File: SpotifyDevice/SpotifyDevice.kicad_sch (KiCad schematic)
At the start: 0 parts

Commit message: Found Draft 1 Parts and imported Libraries
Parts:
- added S1: B3F-4055, ImportedParts:SW_B3F-4055, symbol Imported Parts:B3F-4055
- added U1: ESP32-S3-WROOM-1, RF_Module:ESP32-S3-WROOM-1, symbol RF_Module:ESP32-S3-WROOM-1
- added U2: CR2013-MI2120, Display:CR2013-MI2120, symbol Driver_Display:CR2013-MI2120
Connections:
- new net: S1.1, S1.2
- new net: S1.3, S1.4
- new net: U1.1 (GND), U1.40 (GND), U1.41 (GND)

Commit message: Draft 1 of Schematic Complete
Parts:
- added C1, C2, C4: 0.1 μF, symbol Device:C_Small_US
- added C3: 10 μF, symbol Device:C_Small_US
- added D1: LED, symbol Device:LED
- added R1: 10kΩ, symbol Device:R_Small_US
- added R2: 330Ω, symbol Device:R_Small_US
- added S2, S3, S4, S5: B3F-4055, ImportedParts:SW_B3F-4055, symbol Imported Parts:B3F-4055
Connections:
- net S1: now reaches S1.1, S1.2
- net S1: now also U1.7 (IO7)
- net GND: now reaches S1.3, S1.4
- net GND: now also U1.1 (GND), U1.40 (GND), U1.41 (GND), U2.2 (GND), C1.1, C2.1, C3.1, C4.1, D1.1 (K), S2.3, S2.4, S3.3, S3.4, S4.3, S4.4, S5.3, S5.4
- net S2: now reaches U1.12 (IO8)
- net S2: now also S2.1, S2.2
- net S3: now reaches U1.17 (IO9)
- net S3: now also S3.1, S3.2
- net S4: now reaches U1.18 (IO10)
- net S4: now also S4.1, S4.2
- net S5: now reaches U1.19 (IO11)
- net S5: now also S5.1, S5.2
- net +3.3V: now reaches U1.2 (3V3)
- net +3.3V: now also U2.1 (VCC), U2.8 (LED), C1.2, C2.2, C3.2, R1.2
- net at U1.20 (IO12): now also R2.2
- net MOSI: now reaches U1.28 (IO35)
- net MOSI: now also U2.6 (MOSI)
- net SCK: now reaches U1.29 (IO36)
- net SCK: now also U2.7 (SCK)
- net at U1.3 (EN): now also C4.2, R1.1
- net D/C: now reaches U1.30 (IO37)
- net D/C: now also U2.5 (D/~{C})
- net CS: now reaches U1.31 (IO38)
- net CS: now also U2.3 (~{CS})
- net RESET: now reaches U1.32 (IO39)
- net RESET: now also U2.4 (RESET)
- new net LED: D1.2 (A), R2.1
- no-connect marks 0 -> 31
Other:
- note added: "AddOns"
- note added: "Microcontroller"
- note added: "Screen"
- moved on the sheet: S1, U1, U2

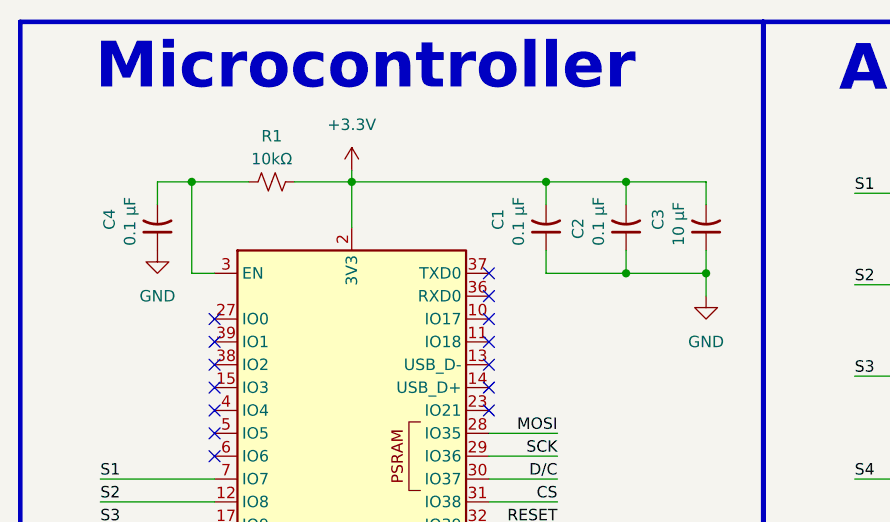
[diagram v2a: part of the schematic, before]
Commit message: Added 3D models and updated SCM
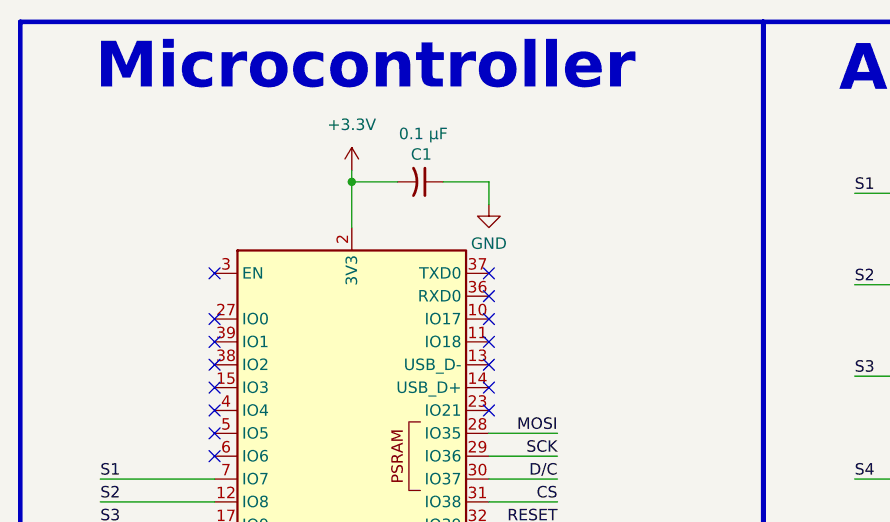
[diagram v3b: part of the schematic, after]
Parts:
- removed C2, C4: 0.1 μF, symbol Device:C_Small_US
- removed C3: 10 μF, symbol Device:C_Small_US
- removed R1: 10kΩ, symbol Device:R_Small_US
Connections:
- no-connect marks 31 -> 32
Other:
- moved on the sheet: C1

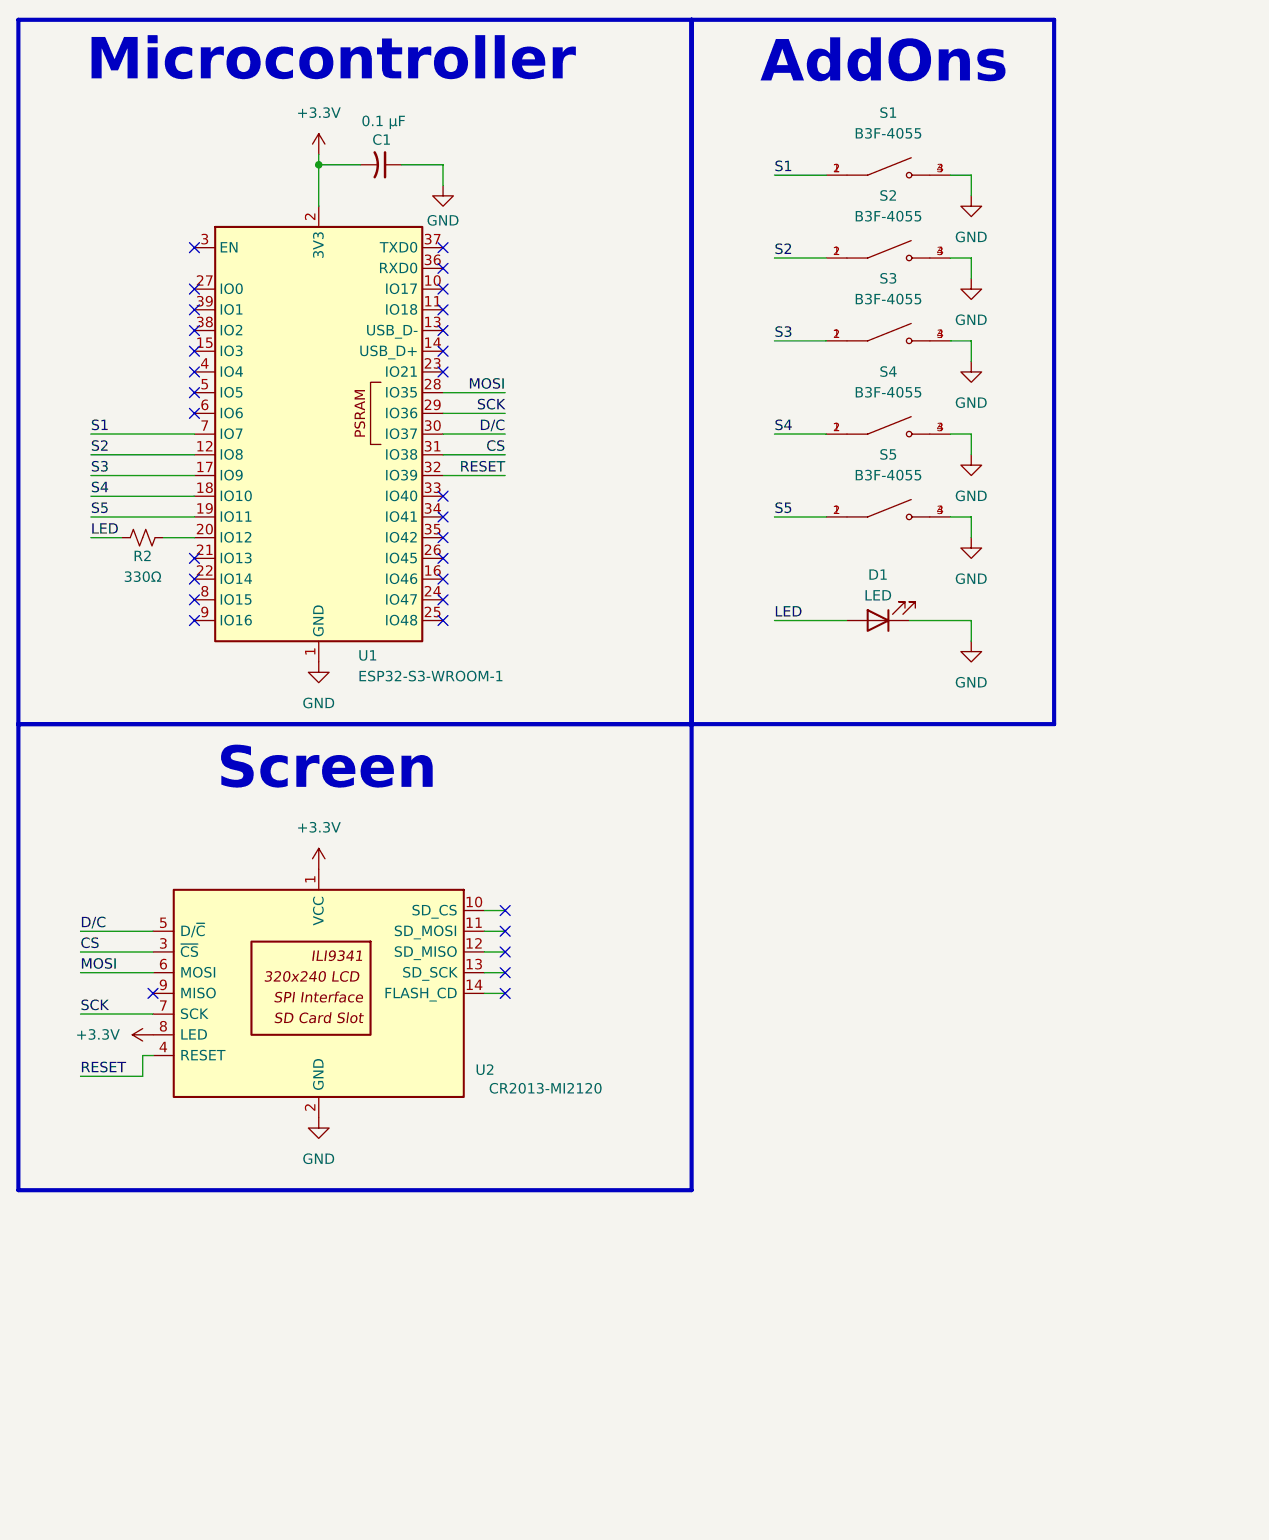
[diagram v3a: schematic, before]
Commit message: updated footprints
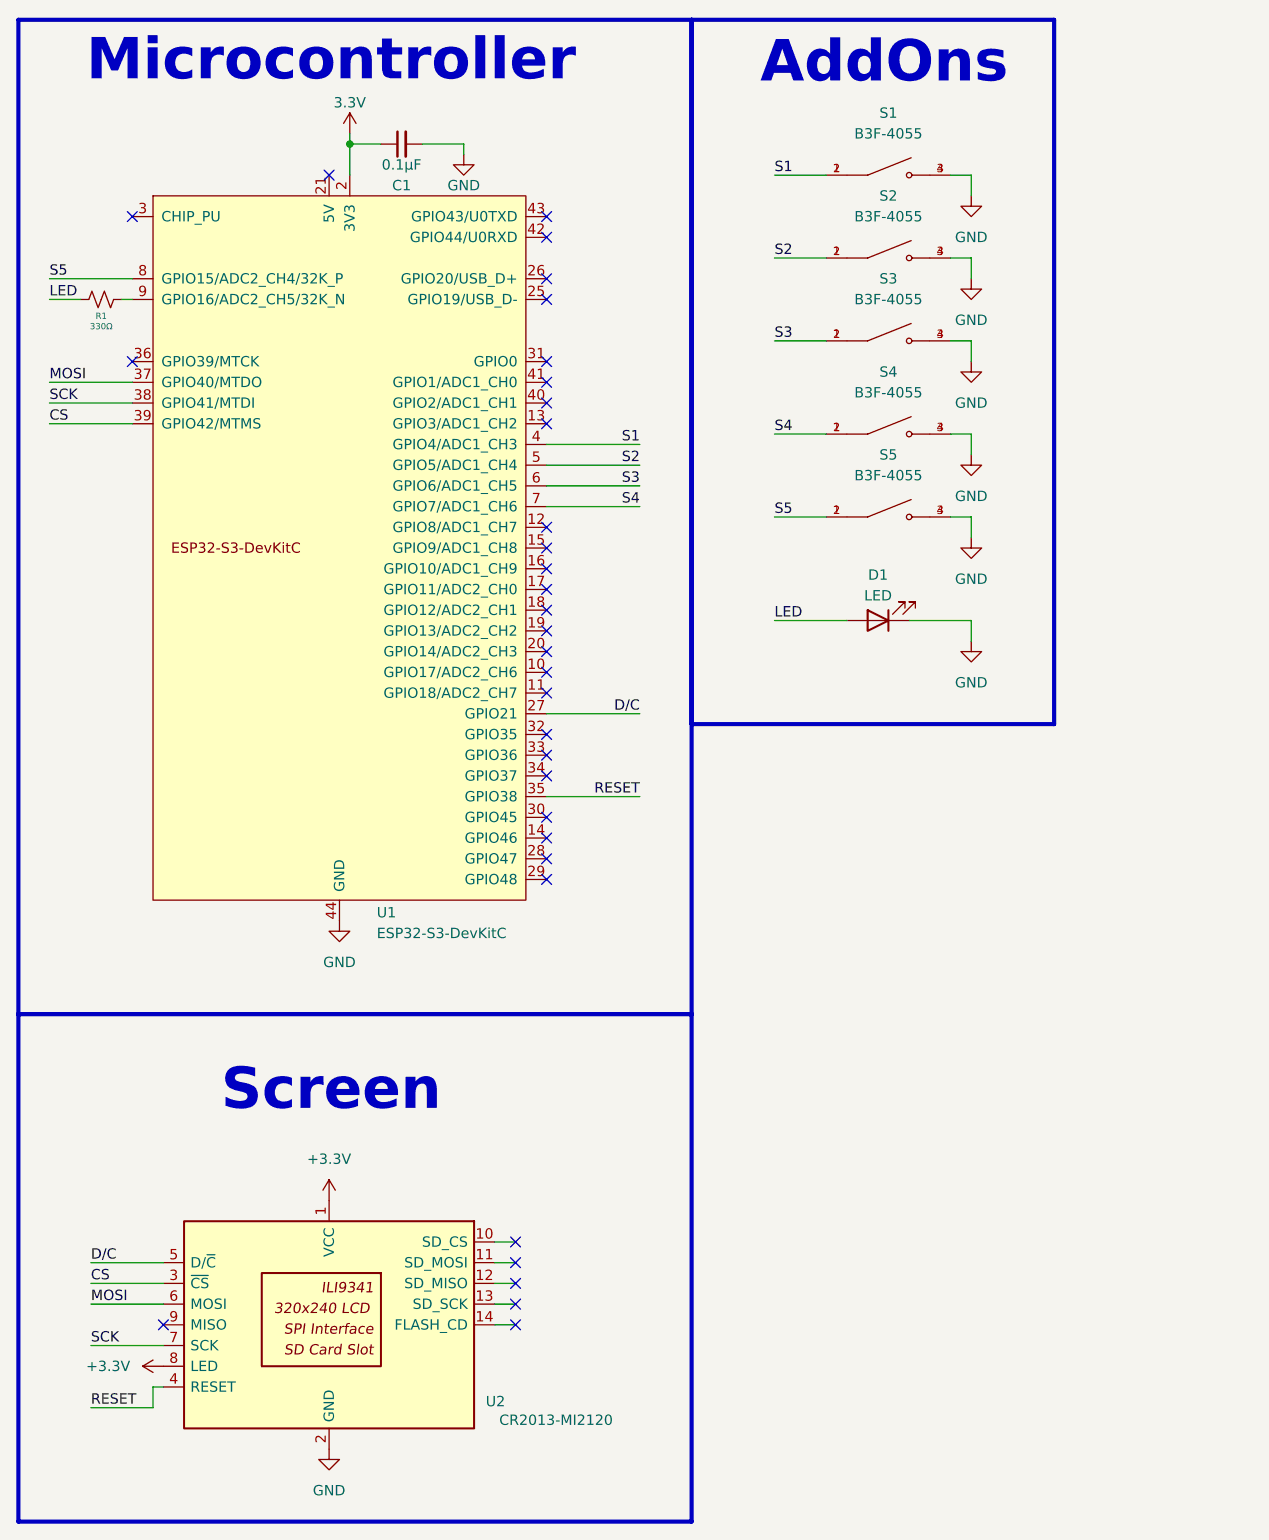
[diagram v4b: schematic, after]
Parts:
- removed C1: 0.1 μF, symbol Device:C_Small_US
- removed R2: 330Ω, symbol Device:R_Small_US
- removed U1: ESP32-S3-WROOM-1, RF_Module:ESP32-S3-WROOM-1, symbol RF_Module:ESP32-S3-WROOM-1
- added C1: 0.1µF, Capacitor_SMD:C_0603_1608Metric_Pad1.08x0.95mm_HandSolder, symbol PCM_SparkFun-Capacitor:C_Small
- added R1: 330Ω, Resistor_SMD:R_0603_1608Metric_Pad0.98x0.95mm_HandSolder, symbol Device:R_Small_US
- added U1: ESP32-S3-DevKitC, Espressif:ESP32-S3-DevKitC-1-N16R8, symbol Expressif:ESP32-S3-DevKitC
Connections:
- net CS: now also U1.39 (GPIO42/MTMS)
- net D/C: now also U1.27 (GPIO21)
- net GND: now also C1.2, U1.22 (GND), U1.23 (GND), U1.24 (GND), U1.44 (GND)
- net LED: now also R1.2
- net MOSI: now also U1.37 (GPIO40/MTDO)
- net RESET: now also U1.35 (GPIO38)
- net S1: now also U1.4 (GPIO4/ADC1_CH3)
- net S2: now also U1.5 (GPIO5/ADC1_CH4)
- net S3: now also U1.6 (GPIO6/ADC1_CH5)
- net S4: now also U1.7 (GPIO7/ADC1_CH6)
- net S5: now also U1.8 (GPIO15/ADC2_CH4/32K_P)
- net SCK: now also U1.38 (GPIO41/MTDI)
- new net: R1.1, U1.9 (GPIO16/ADC2_CH5/32K_N)
- new net 3.3V: C1.1, U1.1 (3V3), U1.2 (3V3)
- no-connect marks 32 -> 33
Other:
- moved on the sheet: U2

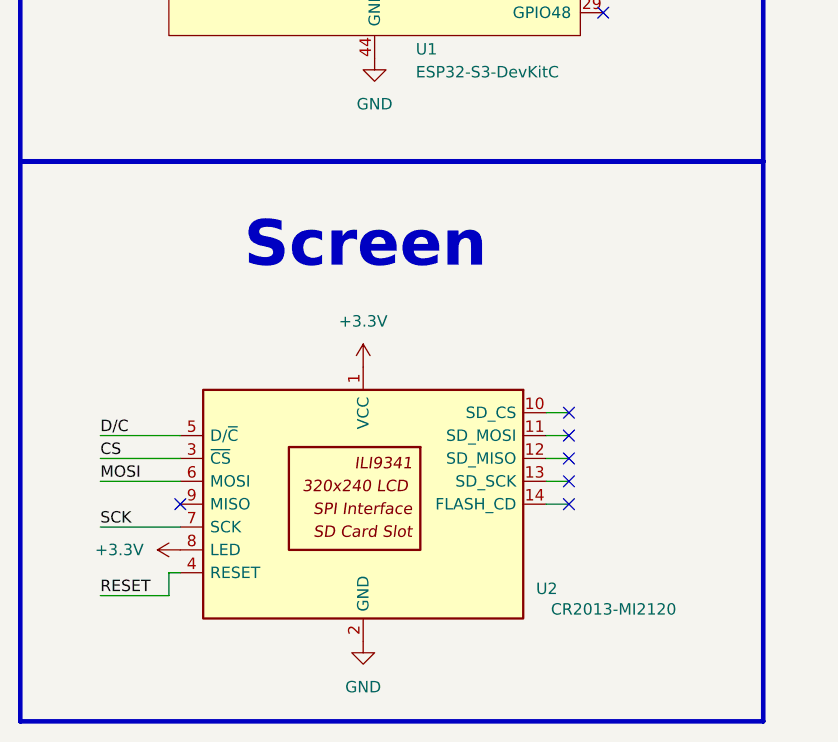
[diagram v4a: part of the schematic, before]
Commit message: Added Footprint & Symbol for screen
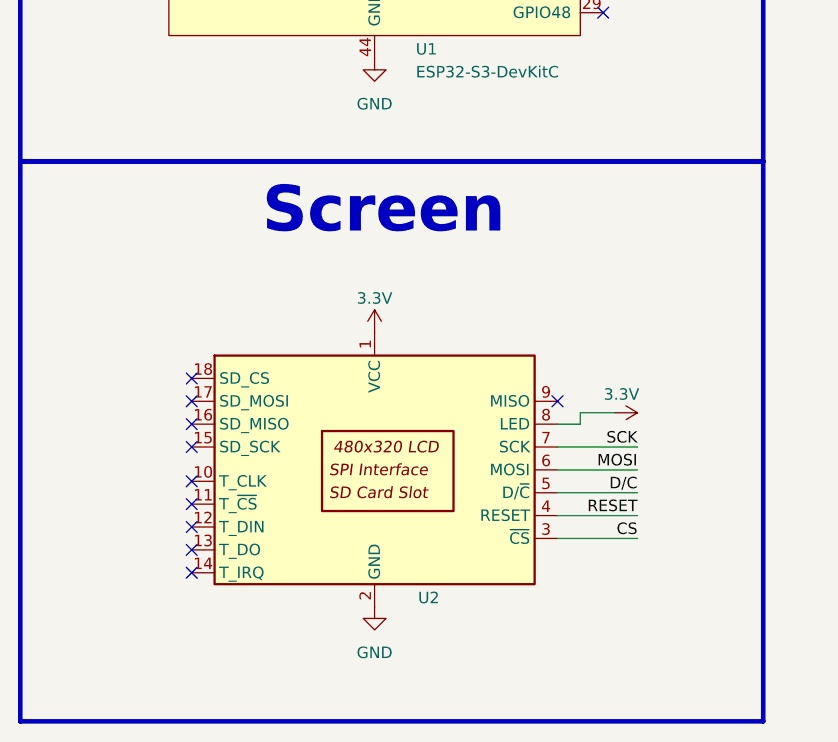
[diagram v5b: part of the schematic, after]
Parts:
- removed U2: CR2013-MI2120, Display:CR2013-MI2120, symbol Driver_Display:CR2013-MI2120
- added U2: ~, symbol Custom_Parts:3.5{dblquote}_TFT_SPI_480x320_Display
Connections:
- net 3.3V: now also U2.1 (VCC), U2.8 (LED)
- net CS: now also U2.3 (~{CS})
- net D/C: now also U2.5 (D/~{C})
- net GND: now also U2.2 (GND)
- net MOSI: now also U2.6 (MOSI)
- net RESET: now also U2.4 (RESET)
- net SCK: now also U2.7 (SCK)
- no-connect marks 33 -> 37

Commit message: Added LED footprints
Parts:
- added D2, D3, D4, D5, D6: LED, Diode_SMD:D_0603_1608Metric, symbol Device:LED
- C1: footprint Capacitor_SMD:C_0603_1608Metric_Pad1.08x0.95mm_HandSolder -> Capacitor_SMD:C_0603_1608Metric
- D1: footprint (none) -> ImportedParts:151031SS06000
- R1: footprint Resistor_SMD:R_0603_1608Metric_Pad0.98x0.95mm_HandSolder -> Resistor_SMD:R_0603_1608Metric
- U2: value ~ -> 3.5" SPI TFT Display; footprint (none) -> ImportedParts:3.5_ SPI TFT Display
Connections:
- net GND: now also D2.1 (K), D3.1 (K), D4.1 (K), D5.1 (K), D6.1 (K)
- net BACKLIGHT: now reaches U1.11 (GPIO18/ADC2_CH7)
- net BACKLIGHT: now also D2.2 (A), D3.2 (A), D4.2 (A), D5.2 (A), D6.2 (A)
- net LED renamed MUTE
- no-connect marks 37 -> 36
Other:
- moved on the sheet: D1

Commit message: Finished PCB and Generated Fab Files
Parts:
- added R2, R3, R4, R5, R6: 100Ω, Resistor_SMD:R_0603_1608Metric, symbol Device:R_Small_US
- D1: value LED -> RED
- D2, D3, D4, D5, D6: value LED -> WHITE; footprint Diode_SMD:D_0603_1608Metric -> ImportedParts:IN-S63BT5UW
- S1, S2, S3, S4, S5: now not fitted; now left out of the parts list
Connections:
- net BACKLIGHT: now also R2.2, R3.2, R4.2, R5.2, R6.2; no longer D2.2 (A), D3.2 (A), D4.2 (A), D5.2 (A), D6.2 (A)
- net CS: now also U1.27 (GPIO21); no longer U1.39 (GPIO42/MTMS)
- net D/C: now also U1.37 (GPIO40/MTDO); no longer U1.27 (GPIO21)
- net GND: now also D1.2 (C); no longer D1.1 (K)
- net MOSI: now also U1.38 (GPIO41/MTDI); no longer U1.37 (GPIO40/MTDO)
- net MUTE: now also U1.9 (GPIO16/ADC2_CH5/32K_N); no longer D1.2 (A)
- net SCK: now also U1.39 (GPIO42/MTMS); no longer U1.38 (GPIO41/MTDI)
- net at R1.1: now also D1.1 (A); no longer U1.9 (GPIO16/ADC2_CH5/32K_N)
- new net: D2.2 (A), R2.1
- new net: D6.2 (A), R6.1
- new net: D4.2 (A), R4.1
- new net: D3.2 (A), R3.1
- new net: D5.2 (A), R5.1
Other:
- moved on the sheet: R1

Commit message: Added 3d models
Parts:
- S1, S2, S3, S4, S5: now fitted; now in the parts list
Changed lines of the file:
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@@
 		(unit 1)
 		(exclude_from_sim no)
-		(in_bom no)
-		(on_board yes)
-		(dnp yes)
+		(in_bom yes)
+		(on_board yes)
+		(dnp no)
 		(fields_autoplaced yes)
 		(property "Reference" "S3"
@@
 		(unit 1)
 		(exclude_from_sim no)
-		(in_bom no)
-		(on_board yes)
-		(dnp yes)
+		(in_bom yes)
+		(on_board yes)
+		(dnp no)
 		(fields_autoplaced yes)
 		(property "Reference" "S1"
@@
 		(unit 1)
 		(exclude_from_sim no)
-		(in_bom no)
-		(on_board yes)
-		(dnp yes)
+		(in_bom yes)
+		(on_board yes)
+		(dnp no)
 		(fields_autoplaced yes)
 		(property "Reference" "S5"
@@
 		(unit 1)
 		(exclude_from_sim no)
-		(in_bom no)
-		(on_board yes)
-		(dnp yes)
+		(in_bom yes)
+		(on_board yes)
+		(dnp no)
 		(fields_autoplaced yes)
 		(property "Reference" "S4"
@@
 		(unit 1)
 		(exclude_from_sim no)
-		(in_bom no)
-		(on_board yes)
-		(dnp yes)
+		(in_bom yes)
+		(on_board yes)
+		(dnp no)
 		(fields_autoplaced yes)
 		(property "Reference" "S2"
